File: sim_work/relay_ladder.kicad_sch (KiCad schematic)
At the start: 22 parts, among them Q1 2N3904, Q2 2N3904, Q3 2N3904, Q4 2N3904, SW1 K1, SW2 K2, SW3 K3, SW4 K4

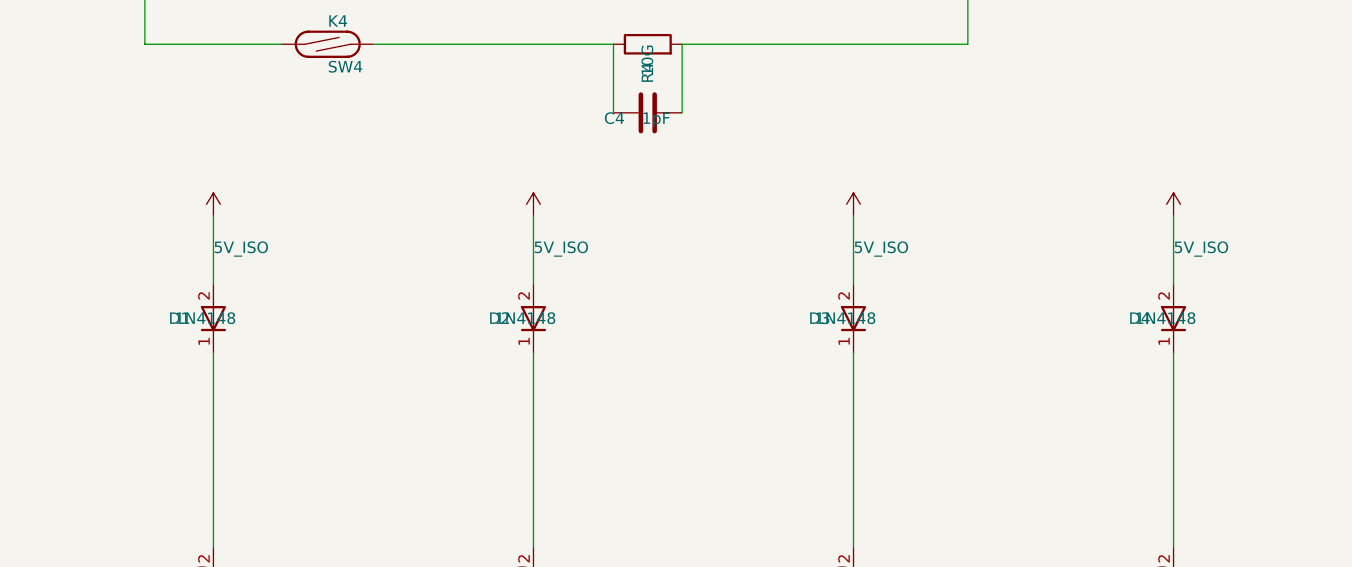
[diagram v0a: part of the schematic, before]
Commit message: Per-block PDF schematics: 6 oscillator + 6 TIA blocks with merged PDFs
Add individual A4 schematic generation for each functional circuit block:
- Oscillator: summing amp, integrator 1/2, RMS detector, power supply, MCU
- TIA: input filters, analog mux, mux TIA, relay ladder, MCU section, electrometer
- merge_pdfs() helper using PyMuPDF for multi-page output
- CLI commands: osc_blocks, tia_blocks
- All blocks verified: 0 wire crossings, complete pin connectivity

Co-Authored-By: Claude Opus 4.6 <noreply@anthropic.com>
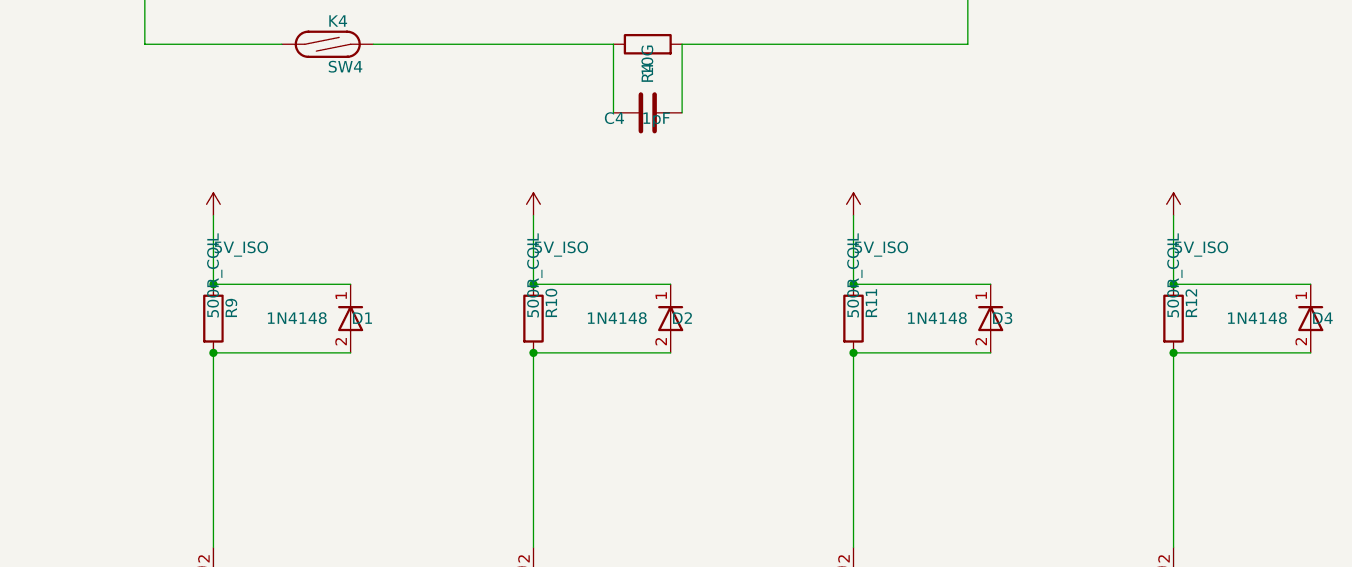
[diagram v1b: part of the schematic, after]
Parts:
- added R10, R11, R12, R9: 500R_COIL, symbol R:R
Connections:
- net 5V_ISO: now also D1.1 (K), D2.1 (K), D3.1 (K), D4.1 (K), R10.1, R11.1, R12.1, R9.1; no longer D1.2 (A), D2.2 (A), D3.2 (A), D4.2 (A)
- net at Q1.2 (C): now also D1.2 (A), R9.2; no longer D1.1 (K)
- net at Q2.2 (C): now also D2.2 (A), R10.2; no longer D2.1 (K)
- net at Q3.2 (C): now also D3.2 (A), R11.2; no longer D3.1 (K)
- net at Q4.2 (C): now also D4.2 (A), R12.2; no longer D4.1 (K)
